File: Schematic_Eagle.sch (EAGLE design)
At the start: 24 parts, among them T1 TIP31C

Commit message: Uploaded new version of schematic
Updated to draft 2, 1/3/17
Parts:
- added JP1, JP2: (no value), pinhead:PINHD-1X2
- added JP3, JP4: (no value), pinhead:PINHD-1X3
- IR1, IR2, IR3, IR4: value TSOP1730TB1 -> TSOP4838
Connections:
- net GND: now also JP1.2, JP2.2
- net N$10: now also JP2.1
- net N$5: now also JP1.1
- net OPTICAL1: now also JP3.3, JP4.3
- net OPTICAL2: now also JP3.2, JP4.2
- net OPTICAL3: now also JP3.1, JP4.1
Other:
- note added: ""Spooky Action" Schematic Draft 2 Jan 3rd, 2017 Design Modifications still to consider: -Adjust breakbeam IR LED freq to 33Khz, and include a 33Khz receiver on same board (removes need for receiver on opposite side of stick). Suggest TSOP4833 as a repacement"
- note added: "'555 Timer to flicker IR LED embedded on glasses at 38 KHz. Vcc = 9V Timer can run from 5V, but have to reduce R3 to maintain current through LED. Jumper intended to illustrate that LED is located off-board and can be disconnected if needed."
- note added: "'555 timer to flicker IR LED associated with beam break at 38KHz. Vcc = 9V Timer can run from 5V, but have to reduce R6 to maintain current through LED. Jumper intended to illustrate that LED is located off-board and can be disconnected if needed."
- note added: "GL Comments: - We should specify a part number for the LEDs"
- note added: "Optical receivers placed around the perimeter of the rotating ball Jumper is a suggestion for ease of connection/disconnection"
- note added: "Strobe trigger: switch closure The output should be terminated with a male, mono, 1/4" phono jack (tip/sleeve)."
- note added: "To strobe jack input (gnd/sleeve)"
- note added: "To strobe jack input (signal/tip)"
- note removed: ""Spooky Action" Schematic Draft 1 Dec 24th, 2016 Design Modifications still to consider: -Adjust breakbeam IR LED freq to 33Khz, and include a 33Khz receiver on same board (removes need for receiver on opposite side of stick)"
- note removed: "'555 Timer to flicker IR LED embedded on glasses at 38 KHz. Vcc = 9V"
- note removed: "'555 timer to flicker IR LED associated with beam break at 38KHz. Vcc = 9V"
- note removed: "Optical receivers placed around the perimeter of the rotating ball"
- note removed: "Strobe trigger: switch closure"
- note removed: "To strobe jack input (gnd)"
- note removed: "To strobe jack input (signal)"
- moved on the sheet: D1, IR1, IR2, IR3, IR4, IRLED1, IRLED2, R7, T1

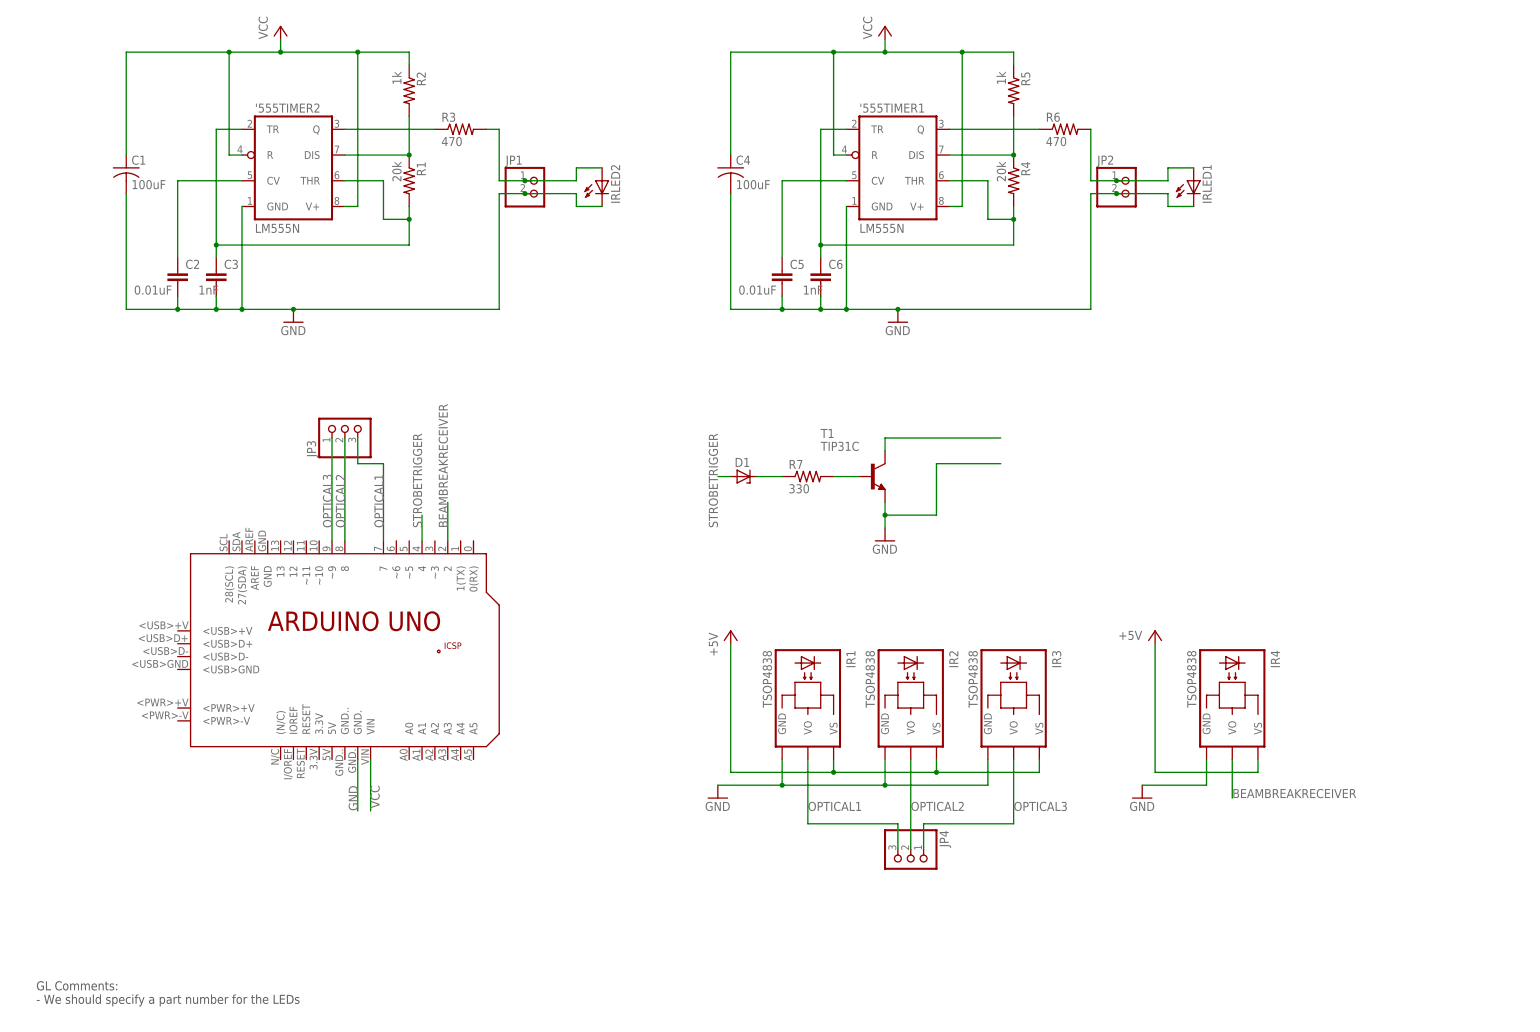
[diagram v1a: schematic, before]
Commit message: Schematic for two balls
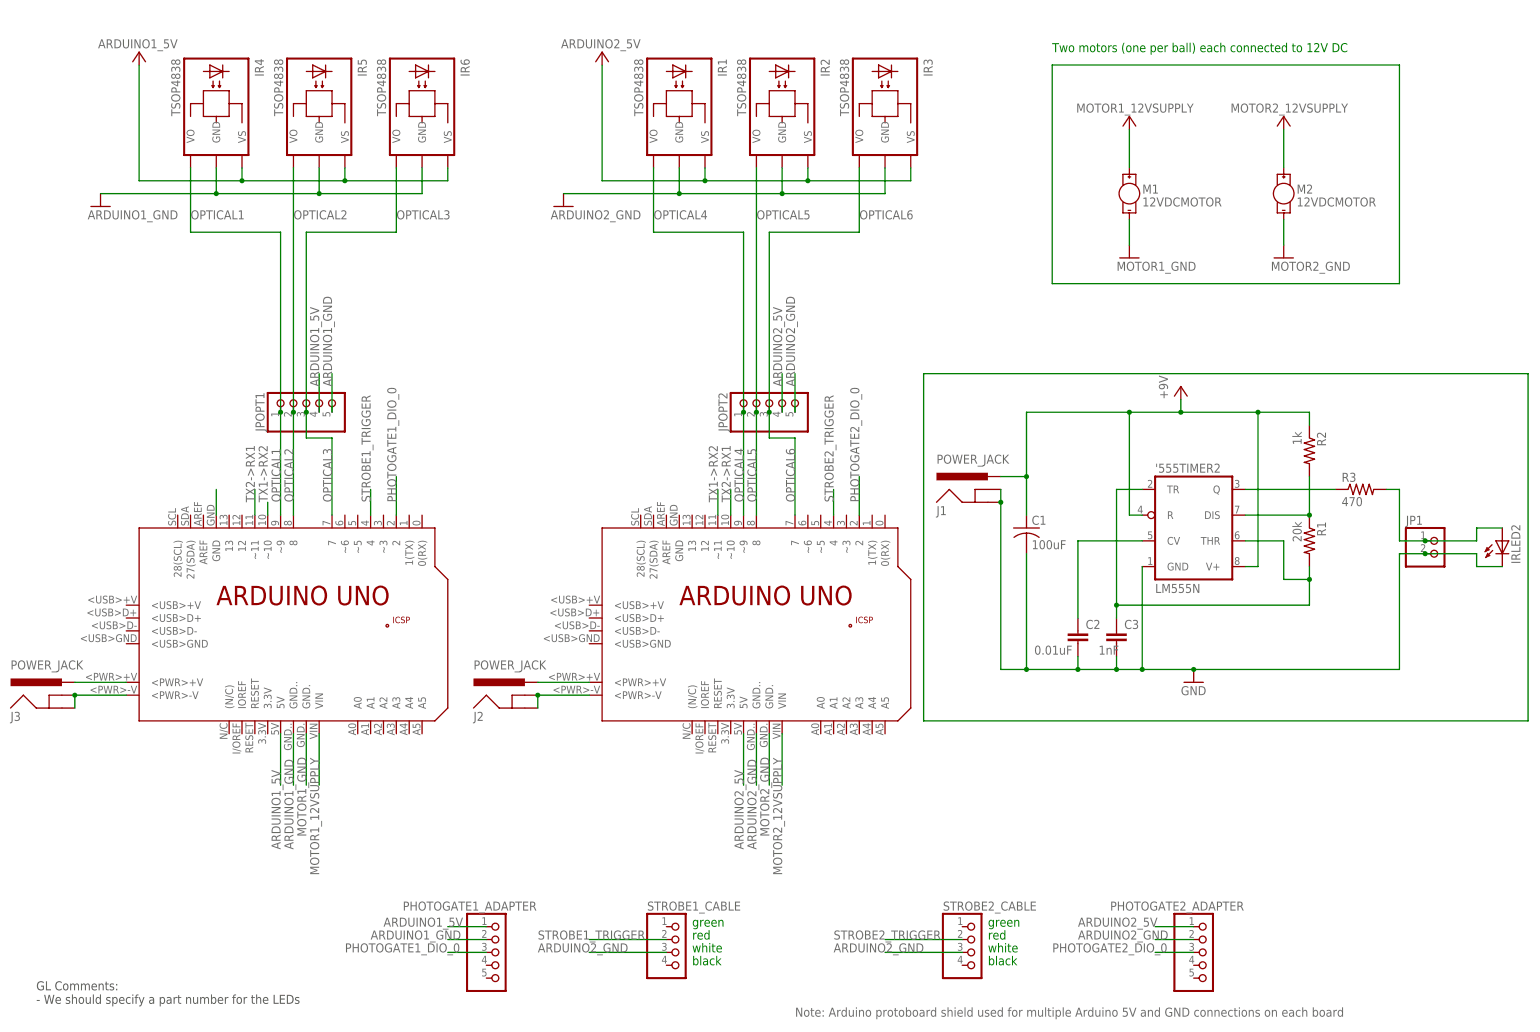
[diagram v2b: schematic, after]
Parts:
- removed '555TIMER1: LM555N, linear:LM555N
- removed C4: 100uF, resistor:C-USC0402
- removed C5: 0.01uF, capacitor-wima:C2,5-3
- removed C6: 1nF, capacitor-wima:C2,5-3
- removed D1: 1N821, diode:1N821
- removed IRLED1: SFH482, led:SFH482
- removed JP2: (no value), pinhead:PINHD-1X2
- removed JP3, JP4: (no value), pinhead:PINHD-1X3
- removed R4: 20k, fab_copy:RES-US1206FAB
- removed R5: 1k, fab_copy:RES-US1206FAB
- removed R6: 470, fab_copy:RES-US1206FAB
- removed R7: 330, fab_copy:RES-US1206FAB
- removed T1: TIP31C, transistor-neu-to92:TIP31C
- added IR5, IR6: TSOP4838, spooky:TSOP1738TB1
- added J1, J2, J3: POWER_JACK, SparkFun-Connectors:POWER_JACK
- added JPOPT1, JPOPT2, PHOTOGATE1_ADAPTER, PHOTOGATE2_ADAPTER: (no value), pinhead:PINHD-1X5
- added M1, M2: 12VDCMOTOR, SparkFun-Electromechanical:MOTOR10MM
- added PCB2: ARDUINO_UNO, E14_Arduino_revC:ARDUINO_UNO
- added STROBE1_CABLE, STROBE2_CABLE: (no value), pinhead:PINHD-1X4
- IR1, IR2, IR3, IR4: device telefunken:TSOP1730TB1 -> spooky:TSOP1738TB1
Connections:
- removed net +5V: IR1.VS, IR2.VS, IR3.VS, IR4.VS
- removed net BEAMBREAKRECEIVER: IR4.VO, PCB1.2
- removed net N$12: D1.C, R7.1
- removed net N$13: R7.2, T1.B
- removed net N$14: T1.C
- removed net N$6: '555TIMER1.Q, R6.1
- removed net N$7: '555TIMER1.DIS, R4.1, R5.2
- removed net STROBETRIGGER: D1.A, PCB1.4
- new net 12VJACK2: J2.PWR, PCB2.<PWR>+V
- new net 12VJACK2(GND): J2.GND, J2.GNDBREAK, PCB2.<PWR>-V
- new net 12VMOTOR1_SUPPLY: M1.+
- new net ARDUINO1_5V: IR4.VS, IR5.VS, IR6.VS, JPOPT1.4, PCB1.5V, PHOTOGATE1_ADAPTER.1
- new net ARDUINO1_GND: IR4.GND, IR5.GND, IR6.GND, JPOPT1.5, PCB1.GND.., PHOTOGATE1_ADAPTER.2
- new net ARDUINO2_5V: IR1.VS, IR2.VS, IR3.VS, JPOPT2.4, PCB2.5V, PHOTOGATE2_ADAPTER.1
- new net ARDUINO2_GND: IR1.GND, IR2.GND, IR3.GND, JPOPT2.5, PCB2.GND.., PHOTOGATE2_ADAPTER.2, STROBE1_CABLE.3, STROBE2_CABLE.3
- new net MOTOR1_12VSUPPLY: PCB1.VIN
- new net MOTOR1_GND: PCB1.GND.
- new net MOTOR2_12VSUPPLY: M2.+, PCB2.VIN
- new net MOTOR2_GND: PCB2.GND.
- new net OPTICAL4: IR1.VO, JPOPT2.1, PCB2.~9
- new net OPTICAL5: IR2.VO, JPOPT2.2, PCB2.8
- new net OPTICAL6: IR3.VO, JPOPT2.3, PCB2.7
- new net PHOTOGATE1_DIO_0: PCB1.2, PHOTOGATE1_ADAPTER.3
- new net PHOTOGATE2_DIO_0: PCB2.2, PHOTOGATE2_ADAPTER.3
- new net STROBE1_TRIGGER: PCB1.4, STROBE1_CABLE.2
- new net STROBE2_TRIGGER: PCB2.4, STROBE2_CABLE.2
- new net TX1->RX2: PCB1.~10, PCB2.~11
- new net TX2->RX1: PCB1.~11, PCB2.~10
- net GND: now also J1.GND, J1.GNDBREAK, M1.-, M2.-; no longer '555TIMER1.GND, C4.2, C5.2, C6.2, IR1.GND, IR2.GND, IR3.GND, IR4.GND, IRLED1.C, JP2.2, PCB1.GND., T1.E
- net N$10: now also PCB1.GND; no longer IRLED1.A, JP2.1, R6.2
- net N$8: now also J3.PWR, PCB1.<PWR>+V; no longer '555TIMER1.THR, '555TIMER1.TR, C6.1, R4.2
- net N$9: now also J3.GND, J3.GNDBREAK, PCB1.<PWR>-V; no longer '555TIMER1.CV, C5.1
- net OPTICAL1: now also IR4.VO, JPOPT1.1, PCB1.~9; no longer IR1.VO, JP3.3, JP4.3, PCB1.7
- net OPTICAL2: now also IR5.VO, JPOPT1.2; no longer IR2.VO, JP3.2, JP4.2
- net OPTICAL3: now also IR6.VO, JPOPT1.3, PCB1.7; no longer IR3.VO, JP3.1, JP4.1, PCB1.~9
- net VCC: now also J1.PWR; no longer '555TIMER1.R, '555TIMER1.V+, C4.1, PCB1.VIN, R5.1
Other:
- note added: ""Spooky Action" Schematic Draft 3 March 14th, 2017"
- note added: "Note: Arduino protoboard shield used for multiple Arduino 5V and GND connections on each board"
- note added: "Two motors (one per ball) each connected to 12V DC"
- note added: "black"
- note added: "green"
- note added: "red"
- note added: "white"
- note removed: ""Spooky Action" Schematic Draft 2 Jan 3rd, 2017 Design Modifications still to consider: -Adjust breakbeam IR LED freq to 33Khz, and include a 33Khz receiver on same board (removes need for receiver on opposite side of stick). Suggest TSOP4833 as a repacement"
- note removed: "'555 timer to flicker IR LED associated with beam break at 38KHz. Vcc = 9V Timer can run from 5V, but have to reduce R6 to maintain current through LED. Jumper intended to illustrate that LED is located off-board and can be disconnected if needed."
- note removed: "Beam break receiver to be placed at opposite side of stick as IR LED"
- note removed: "Strobe trigger: switch closure The output should be terminated with a male, mono, 1/4" phono jack (tip/sleeve)."
- note removed: "To strobe jack input (gnd/sleeve)"
- note removed: "To strobe jack input (signal/tip)"
- moved on the sheet: '555TIMER2, C1, C2, C3, IR1, IR2, IR3, IR4, IRLED2, JP1, R1, R2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
